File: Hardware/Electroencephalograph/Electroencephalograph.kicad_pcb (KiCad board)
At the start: 2 copper layers, 90 x 90 mm, 339 parts, among them J1 Conn_01x08_Male, J2 Conn_01x08_Male, J3 Conn_01x04_Female, J4 Conn_01x04_Female, J5 USB_B_Micro, J6 Conn_01x02_Female, J7 Conn_01x04_Female, J8 Conn_01x02_Male, Q1 FDV304P, Q2 FDV304P, U1 ADS1298IPAG, U10 TPS60403, U11 L78L33_SO8, U12 ESP-12E, U2 OPA330xxD, U3 STM32F030K6Tx, U4 THI3-0511, U5 ADUM2401BRWZ, U6 FT200XD, U7 LP5912-1.8DRVT, U8 LP5912-1.8DRVT, U9 LP5912-1.8DRVT, Y1 20MHz

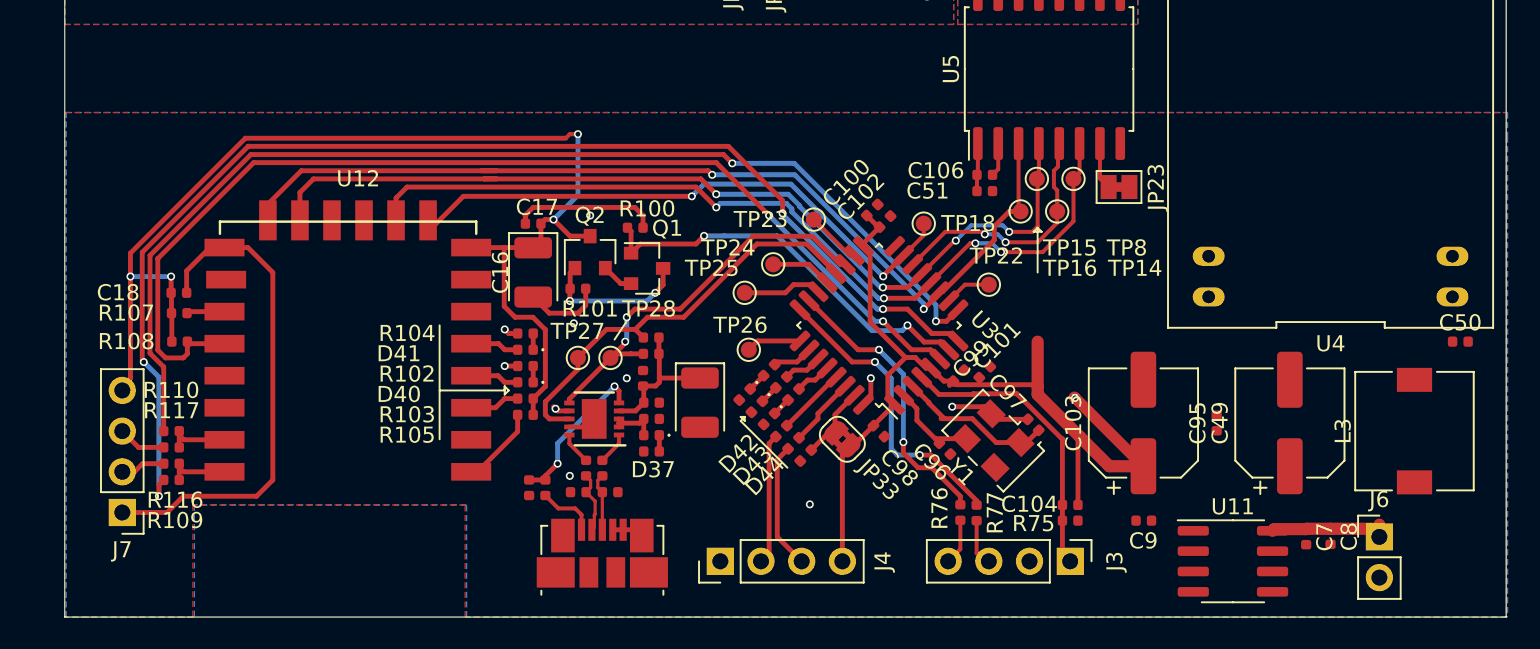
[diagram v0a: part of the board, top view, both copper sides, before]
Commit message: Merge pull request #71 from RobertGawron/feature/draft_of_hardware
Add draft of poqer supply routing for digital part.
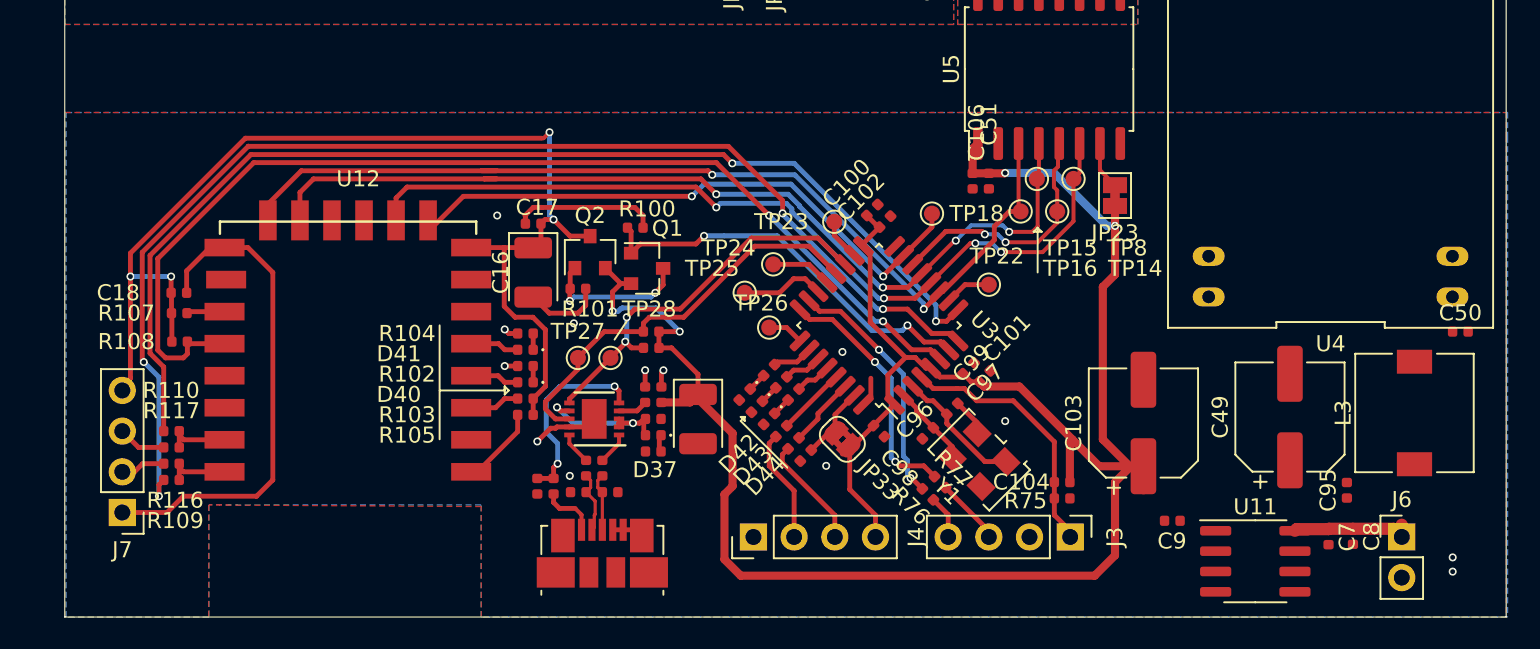
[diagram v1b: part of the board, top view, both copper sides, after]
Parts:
- moved C95 9.15 mm to (130.1, 92.1)
- moved C97 5.15 mm to (105.4, 87.0), turned to 225 degrees
- moved R77 2.98 mm to (104.7, 91.6), turned to 315 degrees
- moved J4 2.57 mm to (93.0, 95.0)
- moved R76 2.32 mm to (103.9, 92.3), turned to 315 degrees
- moved TP26 1.88 mm to (94.0, 81.9)
- moved C9 1.78 mm to (119.2, 94.0)
- moved J3 1.52 mm to (112.8, 95.0)
- moved R75 1.51 mm to (112.3, 91.6)
- moved Y1 1.48 mm to (107.1, 90.2)
- moved C104 1.48 mm to (112.3, 92.6)
- moved C96 1.43 mm to (103.9, 88.5), turned to 45 degrees
- moved C7 1.40 mm to (128.9, 95.0)
- moved C8 1.40 mm to (130.4, 95.0)
- moved J6 1.40 mm to (133.5, 95.0)
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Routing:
- net DP_VDD: track 71.2 -> 139.5 mm, vias 1 -> 4
- net Net-(C109-Pad2): track 4.27 -> 9.18 mm, vias 1 -> 2
- net /DataProcessing/SWCLK: track 18.9 -> 15.7 mm
- net /DataProcessing/SWDIO: track 18.0 -> 15.5 mm
- net Net-(R78-Pad2): track 9.79 -> 12.1 mm
- net Net-(C16-Pad1): track 74.5 -> 72.4 mm
- net /DataProcessing/NRST: track 18.3 -> 16.3 mm
- net Net-(C97-Pad2): track 9.87 -> 8.10 mm
- net Net-(J3-Pad3): track 3.00 -> 4.20 mm
- net Net-(TP26-Pad1): track 3.42 -> 2.27 mm
- net Net-(J4-Pad2): track 8.17 -> 7.08 mm
- net Net-(J4-Pad3): track 7.93 -> 7.01 mm
- net CS_ESP: track 38.3 -> 39.1 mm
- net Net-(TP23-Pad1): track 3.45 -> 2.62 mm
- net SDA: track 26.6 -> 25.8 mm
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
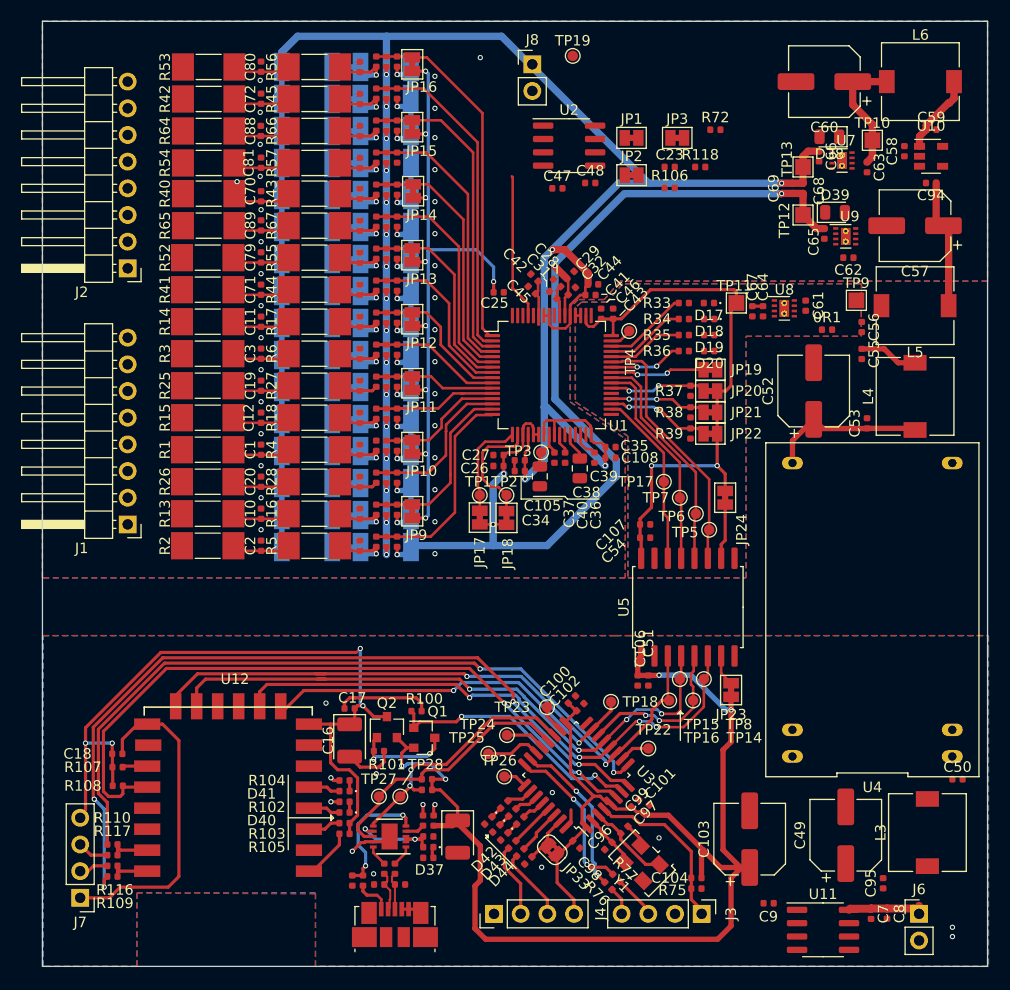
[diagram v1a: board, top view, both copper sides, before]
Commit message: choosed other stgabilisators due to obscolence of previous ones
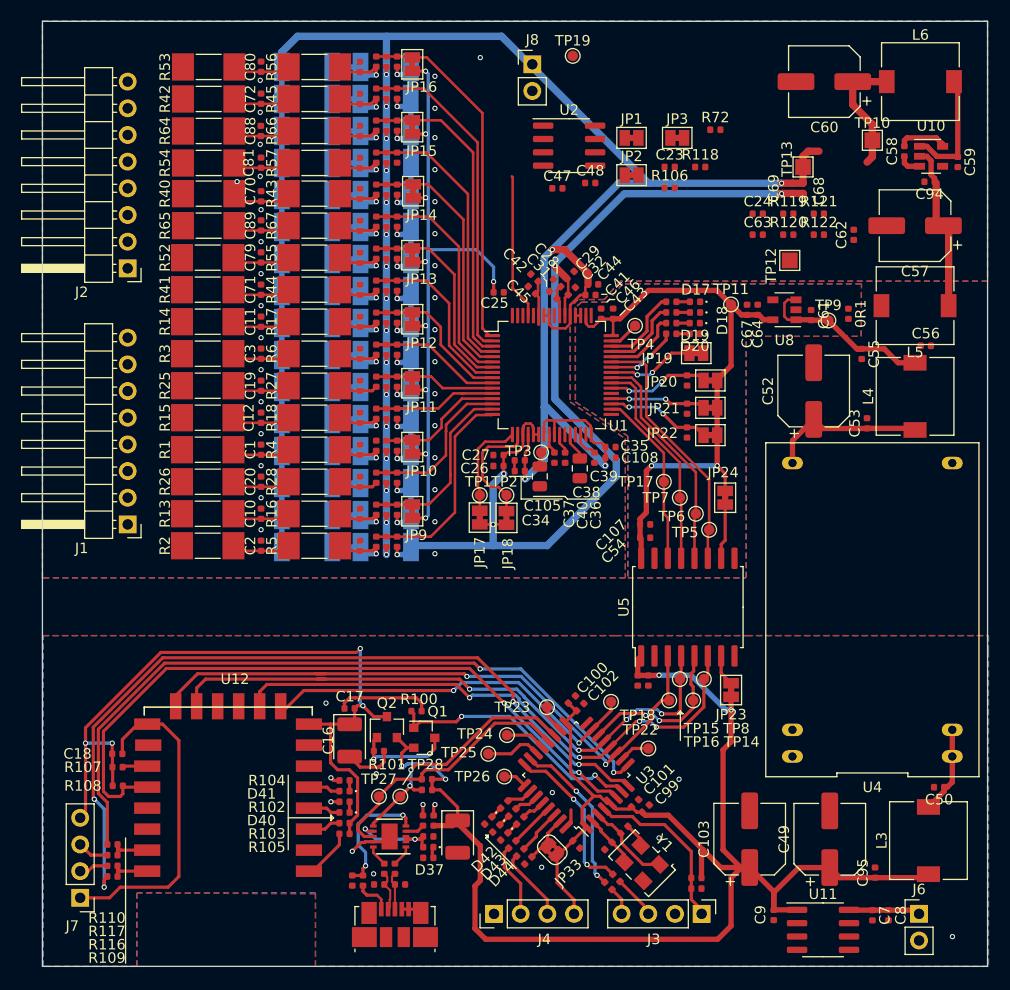
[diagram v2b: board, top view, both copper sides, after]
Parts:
- removed C65, C66: 2u2, Capacitor_SMD:C_0402_1005Metric
- removed D38, D39: D_Schottky, Diode_SMD:D_0805_2012Metric
- removed U7, U9: LP5912-1.8DRVT, Package_SON:WSON-8-1EP_2x2mm_P0.5mm_EP0.9x1.6mm_ThermalVias
- added C24: TBD, Capacitor_SMD:C_0402_1005Metric, F.Cu at (118.1, 28.3)
- added R119: TBD, Resistor_SMD:R_0402_1005Metric, F.Cu at (121.0, 28.3)
- added R120: TBD, Resistor_SMD:R_0402_1005Metric, F.Cu at (121.0, 30.3)
- added R121: TBD, Resistor_SMD:R_0402_1005Metric, F.Cu at (123.9, 28.3)
- added R122: TBD, Resistor_SMD:R_0402_1005Metric, F.Cu at (123.9, 30.3)
- C62, C63: value 2u2 -> TBD
- TP11, TP9: footprint TestPoint:TestPoint_Pad_1.5x1.5mm -> TestPoint:TestPoint_Pad_D1.0mm
- U8: value LP5912-1.8DRVT -> TPS7A20; footprint Package_SON:WSON-8-1EP_2x2mm_P0.5mm_EP0.9x1.6mm_ThermalVias -> Package_TO_SOT_SMD:SOT-23-5
- moved C63 12.2 mm to (118.1, 30.3), turned to 0 degrees
- moved C56 6.36 mm to (134.1, 40.9), turned to 0 degrees
- moved TP12 4.51 mm to (121.2, 32.8)
- moved C59 3.98 mm to (137.2, 23.4), turned to 270 degrees
- moved TP9 3.28 mm to (124.8, 38.5)
- moved 0R1 2.54 mm to (126.8, 37.9), turned to 270 degrees
- moved C62 2.23 mm to (127.3, 30.3), turned to 90 degrees
- moved D20 2.14 mm to (112.1, 39.8)
- moved JP19 2.07 mm to (112.3, 41.6)
- moved R36 2.03 mm to (109.9, 39.8)
- moved C50 1.91 mm to (135.4, 82.9), turned to 180 degrees
- moved D19 1.78 mm to (112.1, 38.7)
- moved R35 1.65 mm to (109.9, 38.7)
- moved C49 1.57 mm to (125.0, 87.9)
- moved D18 1.48 mm to (112.1, 37.7)
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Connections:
- U8 pad 1: D_VDD -> ECC_POWER_SUPPLY
- U8 pad 2: (no net) -> D_GND
- U8 pad 3: D_GND -> ECC_POWER_SUPPLY
- U8 pad 4: ECC_POWER_SUPPLY -> D_GND
- U8 pad 5: D_GND -> D_VDD
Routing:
- net DP_VDD: track 139.5 -> 164.6 mm
- net ECC_POWER_SUPPLY: track 5.63 -> 16.8 mm
- net Net-(C50-Pad1): track 0.00 -> 8.45 mm
- net Net-(C58-Pad2): track 0.00 -> 4.74 mm
- net A_VDD: track 180.7 -> 176.3 mm
- net Net-(C59-Pad1): track 7.58 -> 11.4 mm
- net Net-(C57-Pad1): track 12.2 -> 15.6 mm
- net Net-(C58-Pad1): track 0.00 -> 2.21 mm
- net Net-(D18-Pad2): track 0.00 -> 1.29 mm
- net Net-(D17-Pad2): track 0.00 -> 1.29 mm
- net Net-(D20-Pad2): track 0.00 -> 1.27 mm
- net Net-(D19-Pad2): track 0.00 -> 1.27 mm
- net D_VDD: track 56.5 -> 57.6 mm
- net +9V: track 7.69 -> 6.83 mm
- net Net-(TP4-Pad1): track 2.14 -> 2.86 mm
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
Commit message: Finished design of PCB.
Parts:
- removed R119, R120, R121, R122: TBD, Resistor_SMD:R_0402_1005Metric
- removed TP12: TestPoint, TestPoint:TestPoint_Pad_1.5x1.5mm
- added C65: 10n, Capacitor_SMD:C_0402_1005Metric, F.Cu at (122.3, 24.3)
- added C66: 2u2, Capacitor_SMD:C_0402_1005Metric, F.Cu at (122.3, 26.3)
- added C76: 100n, Capacitor_SMD:C_0402_1005Metric, F.Cu at (121.2, 26.3)
- added C77: 2u2, Capacitor_SMD:C_0402_1005Metric, F.Cu at (127.6, 26.3)
- added JP4: Jumper_NC_Small, Jumper:SolderJumper-2_P1.3mm_Bridged_Pad1.0x1.5mm, F.Cu at (126.4, 22.5)
- added TP20: TestPoint, TestPoint:TestPoint_Pad_D1.0mm, F.Cu at (119.6, 28.7)
- added U7: TPS7A20, Package_TO_SOT_SMD:SOT-23-5, F.Cu at (125.0, 29.7)
- added U9: TPS72325DBVT, Package_TO_SOT_SMD:SOT-23-5, F.Cu at (125.0, 25.7)
- C24, C63: value TBD -> 2u2
- C62: value TBD -> 100n
- TP10, TP13: footprint TestPoint:TestPoint_Pad_1.5x1.5mm -> TestPoint:TestPoint_Pad_D1.0mm
- moved TP19 19.3 mm to (96.1, 32.1)
- moved R118 17.9 mm to (94.7, 23.9), turned to 180 degrees
- moved JP3 16.1 mm to (95.3, 26.4), turned to 90 degrees
- moved R72 14.9 mm to (101.8, 28.7)
- moved C23 13.0 mm to (96.8, 23.9)
- moved C47 12.5 mm to (111.5, 26.3), turned to 90 degrees
- moved J8 11.6 mm to (104.5, 22.6), turned to 270 degrees
- moved R106 11.0 mm to (98.9, 23.9)
- moved U2 9.05 mm to (107.1, 27.7)
- moved JP1 9.03 mm to (98.8, 26.4), turned to 90 degrees
- moved C63 6.89 mm to (124.7, 32.3)
- moved C62 6.15 mm to (121.3, 28.8), turned to 270 degrees
- moved C56 5.01 mm to (129.2, 41.7), turned to 270 degrees
- moved C69 4.98 mm to (116.7, 27.6)
- moved JP2 4.95 mm to (101.5, 26.4), turned to 270 degrees
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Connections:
- C24 pad 1: Net-(C24-Pad1) -> A_VDD
- C62 pad 1: ECC_POWER_SUPPLY -> A_VDD
- C63 pad 1: Net-(C60-Pad1) -> ECC_POWER_SUPPLY
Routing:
- net A_GND: track 0.91 -> 65.3 mm, vias 32 -> 105
- net ECC_POWER_SUPPLY: track 16.8 -> 41.0 mm
- net A_VDD: track 176.3 -> 195.7 mm, vias 19 -> 21
- net Net-(R118-Pad2): track 0.00 -> 15.2 mm
- net Net-(C23-Pad1): track 0.00 -> 12.9 mm
- net Net-(JP3-Pad1): track 0.00 -> 12.5 mm
- net A_VSS: track 244.2 -> 256.3 mm, vias 20 -> 21
- net Net-(J8-Pad1): track 0.00 -> 12.0 mm
- net Net-(TP19-Pad1): track 0.00 -> 6.89 mm
- net Net-(C60-Pad1): track 11.9 -> 18.4 mm
- net /EEGFrontendElectrode5To8/ELECTRODE_1: track 0.00 -> 6.01 mm
- net /EEGFrontendElectrode1To4/ELECTRODE_1: track 0.00 -> 6.01 mm
- net /EEGFrontendElectrode5To8/ELECTRODE_8: track 0.00 -> 5.84 mm
- net /EEGFrontendElectrode5To8/ELECTRODE_2: track 0.00 -> 5.80 mm
- net /EEGFrontendElectrode1To4/ELECTRODE_8: track 0.00 -> 5.80 mm
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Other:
- board text added: "Electroencephalograph rev 1.0"

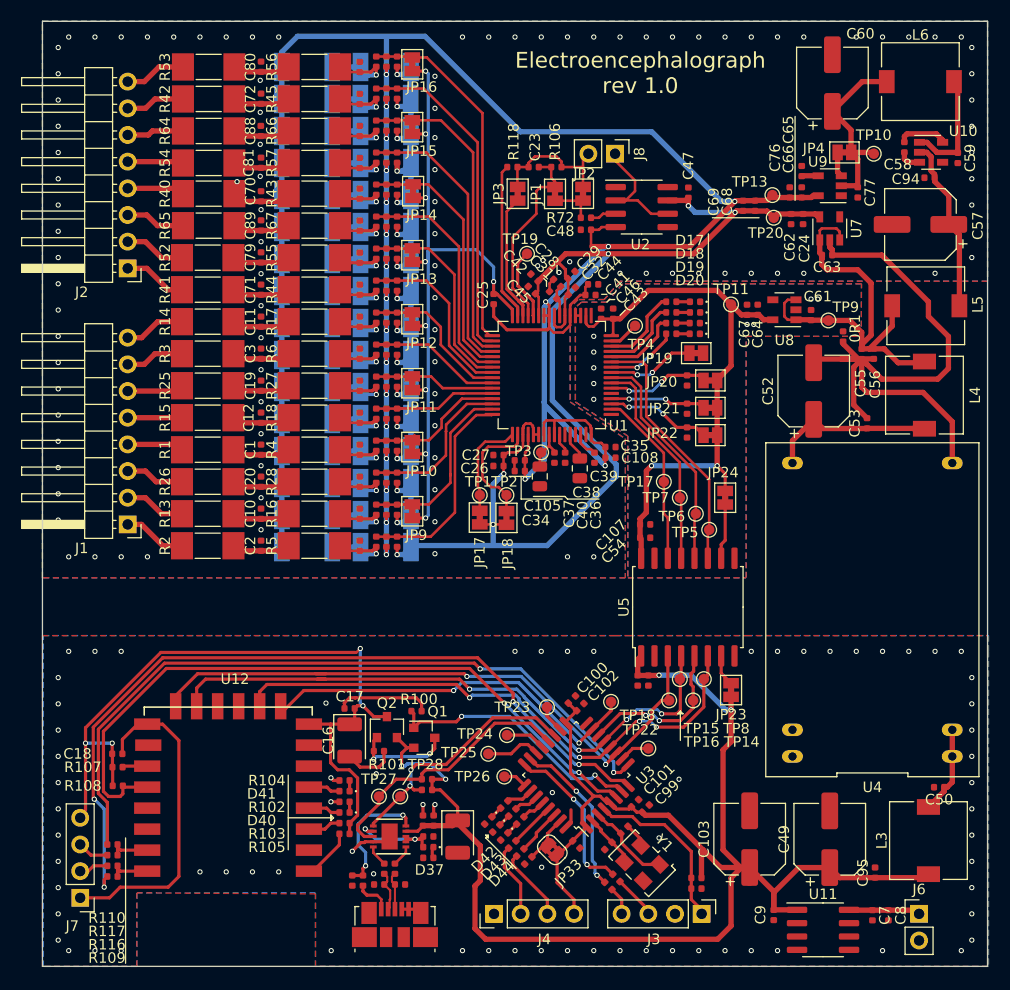
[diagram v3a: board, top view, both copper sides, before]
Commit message: add bom
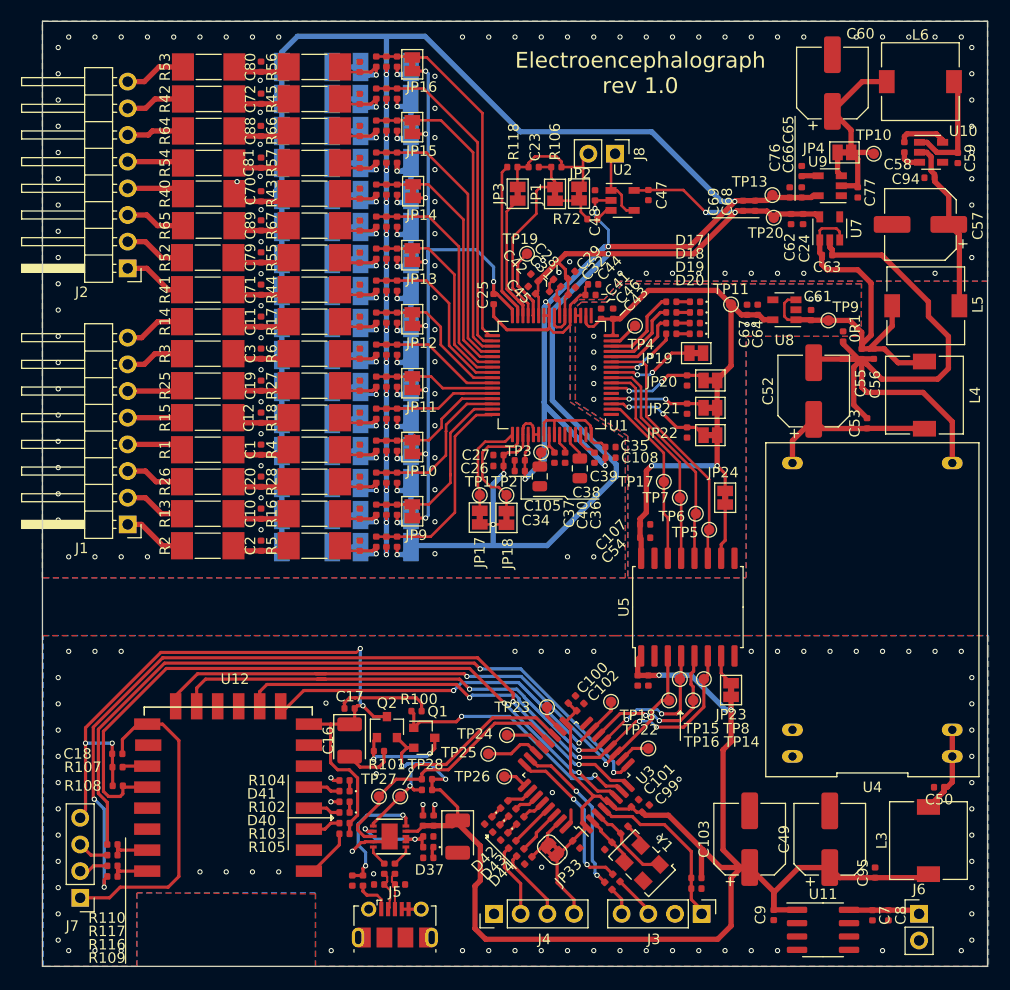
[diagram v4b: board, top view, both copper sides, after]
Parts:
- J5: footprint Connector_USB:USB_Micro-B_Molex_47346-0001 -> Connector_USB:USB_Micro-B_Molex-105017-0001
- U2: value OPA330xxD -> OPA330xxDBV; footprint Package_SO:SOIC-8_3.9x4.9mm_P1.27mm -> Package_TO_SOT_SMD:SOT-23-5
- moved C47 3.82 mm to (107.7, 26.6), turned to 270 degrees
- moved C48 3.39 mm to (102.6, 26.6), turned to 90 degrees
- moved U2 1.93 mm to (105.2, 27.1)
- moved R72 0.63 mm to (102.4, 28.8)
- moved JP2 0.38 mm to (101.1, 26.4)
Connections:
- U2 pad 1: (no net) -> Net-(J8-Pad1)
- U2 pad 2: Net-(J8-Pad1) -> A_VSS
- U2 pad 4: A_VSS -> Net-(J8-Pad1)
- U2 pad 5: (no net) -> A_VDD
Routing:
- net Net-(J8-Pad1): track 12.0 -> 7.87 mm
- net A_VDD: track 195.7 -> 198.6 mm
- net Net-(R72-Pad2): track 2.51 -> 1.64 mm
- net A_VSS: track 256.3 -> 257.2 mm, vias 21 -> 22

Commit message: cleanup after transition to KiCad6
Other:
- net class Default removed
- net class power_supply removed
